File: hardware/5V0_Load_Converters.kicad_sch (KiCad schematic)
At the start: 77 parts, among them J19 61300311121, Q26 EPC2016C, Q27 EPC2016C, Q8 SI2302DDS-T1-GE3, U21 INA199C3DCKR, U30 LTC3833EUDC-TRPBF

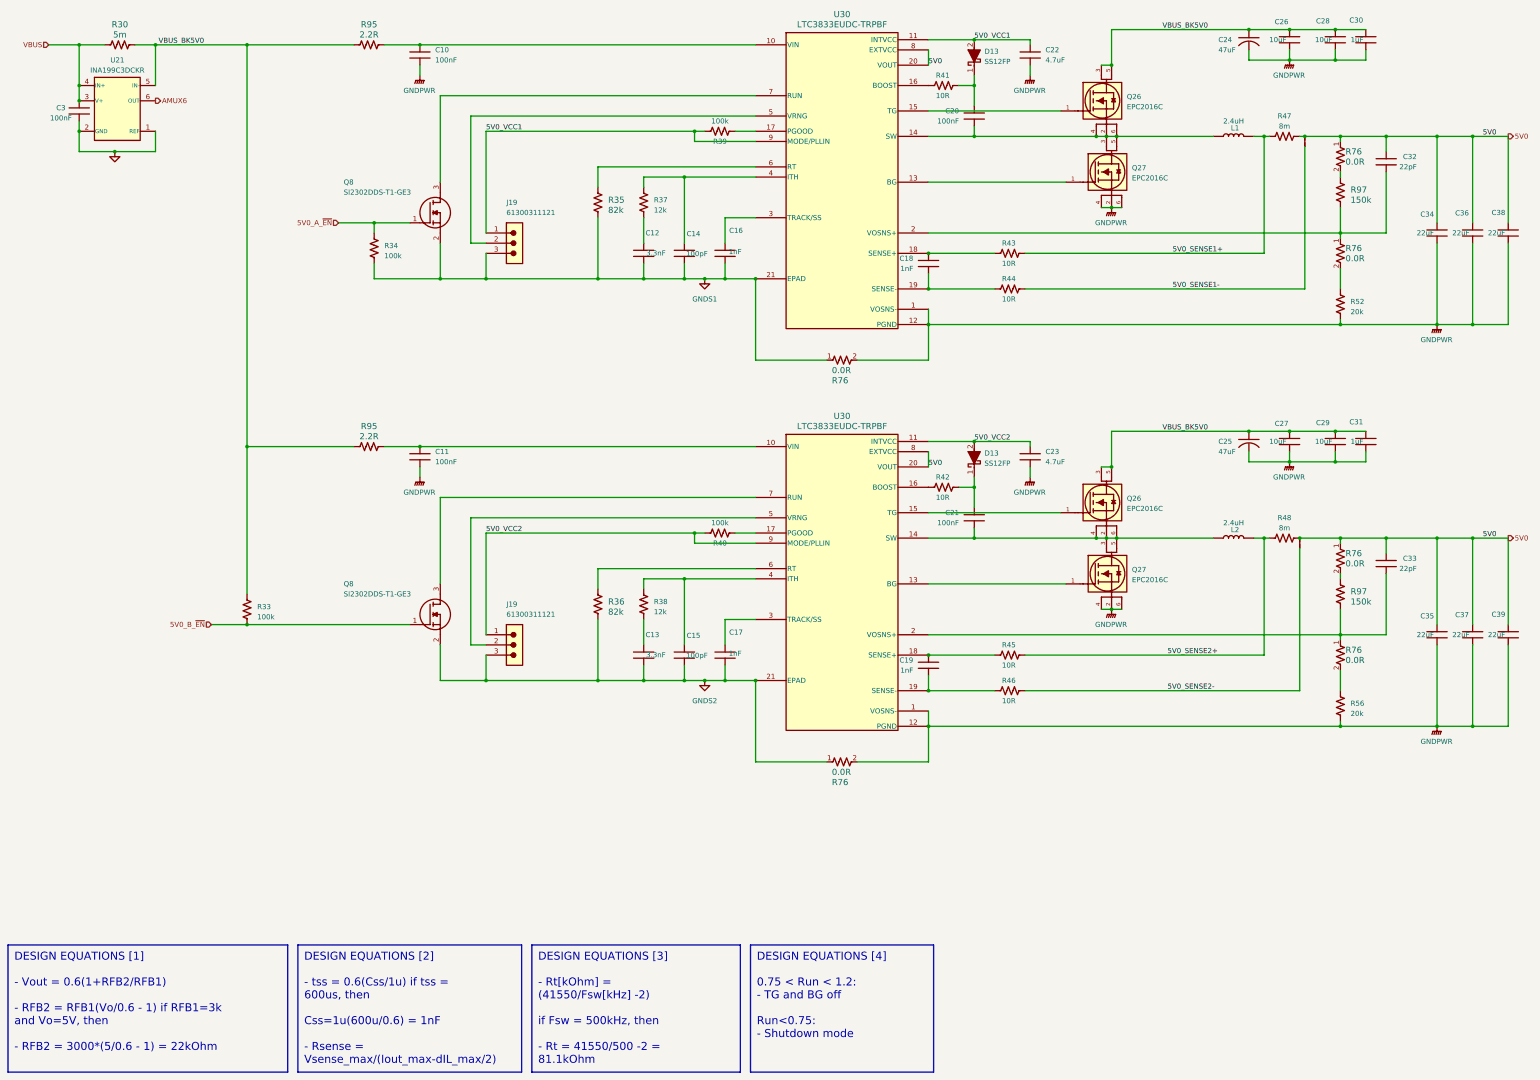
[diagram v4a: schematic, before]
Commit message: hardware: Updating the MPPT circuit.
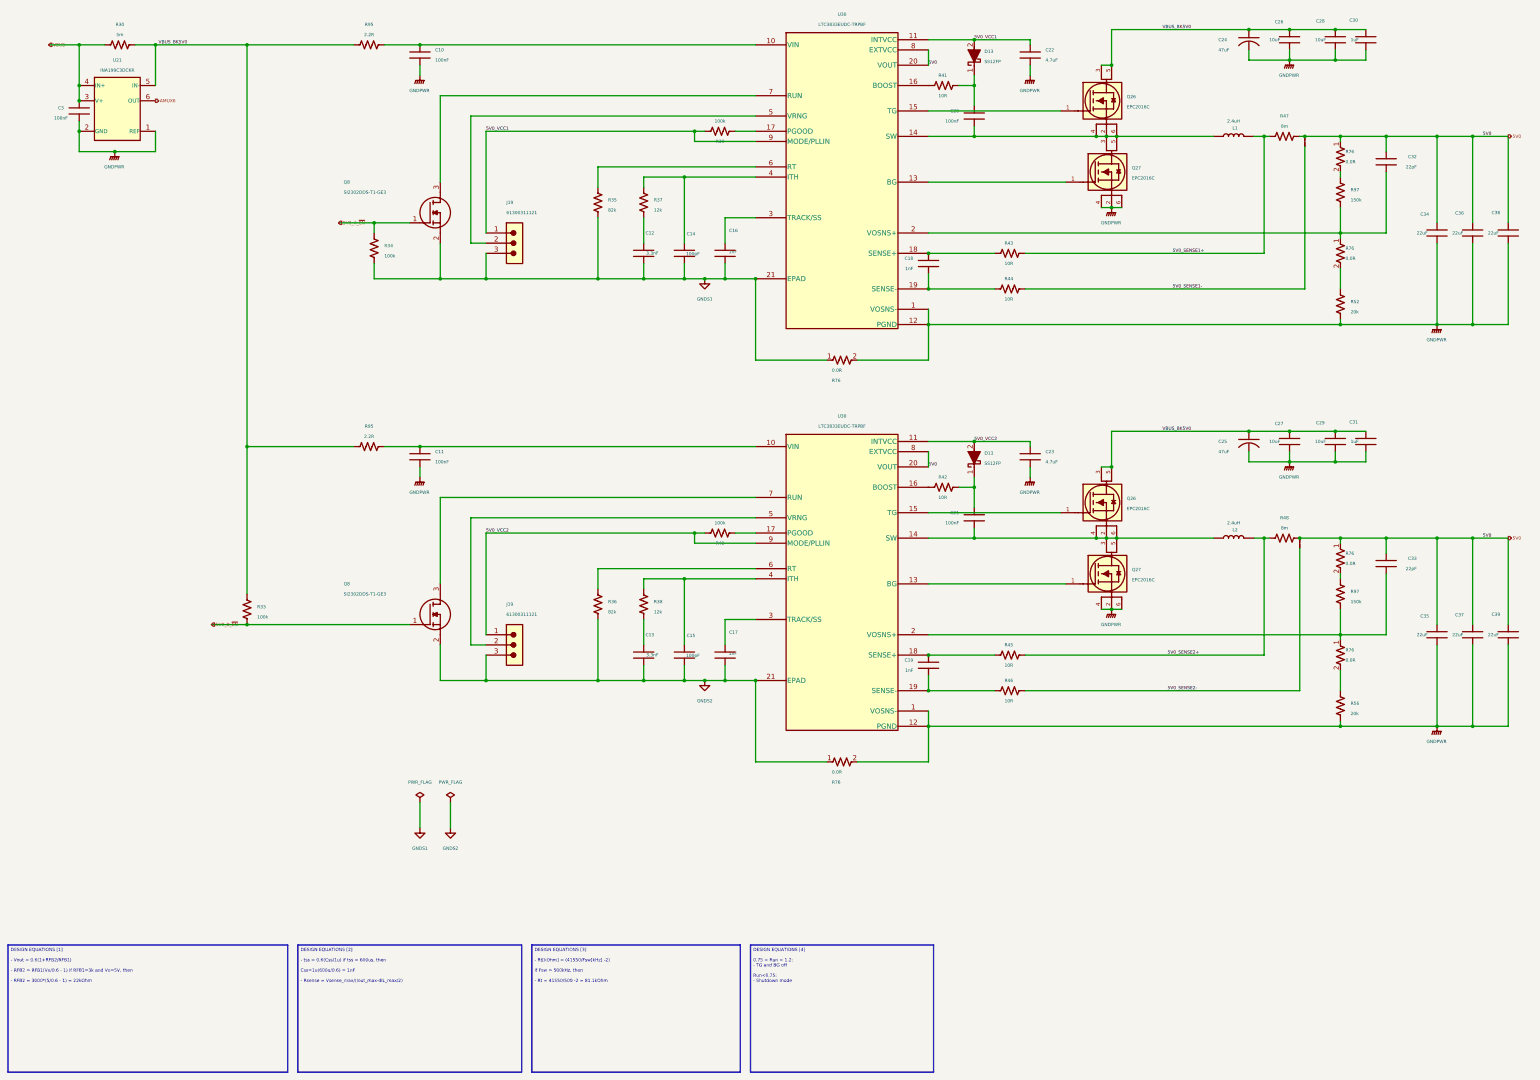
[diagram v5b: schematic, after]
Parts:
- JP1, JP2: symbol Jumper:Jumper -> JUMPER:JUMPER
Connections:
- net GND is gone; now on net GNDPWR: C3.2, U21.1 (REF), U21.2 (GND)

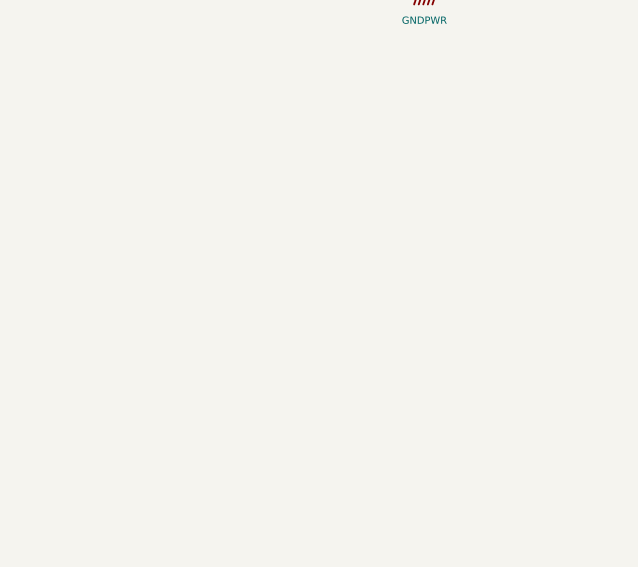
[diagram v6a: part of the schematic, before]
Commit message: hardware: Updating the custom design rules and library.
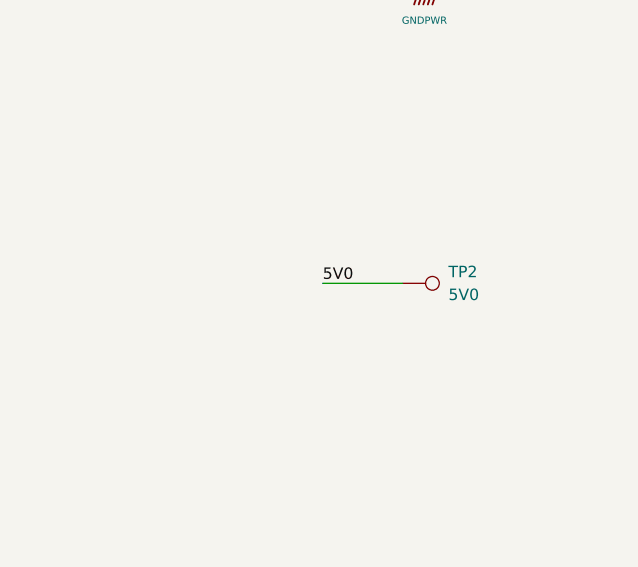
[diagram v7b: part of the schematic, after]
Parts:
- added TP2: 5V0, TestPoint:TestPoint_Pad_D1.0mm, symbol TESTPOINT:TestPoint
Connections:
- net 5V0: now also TP2.1
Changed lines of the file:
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@@
     (stroke (width 0) (type default))
   )
+  (wire (pts (xy 360.68 228.6) (xy 369.57 228.6))
+    (stroke (width 0.5) (type default))
+  )
   (wire (pts (xy 269.24 77.47) (xy 328.93 77.47))
     (stroke (width 0) (type default))
@@
     (effects (font (size 0.8 0.8)) (justify left bottom))
   )
+  (label "5V0" (at 360.68 228.6 0) (fields_autoplaced)
+    (effects (font (size 1.27 1.27)) (justify left bottom))
+  )
   (label "5V0" (at 245.11 130.81 0) (fields_autoplaced)
     (effects (font (size 0.8 0.8)) (justify left bottom))
@@
         )
       )
+    )
+  )
+  (symbol (lib_id "TESTPOINT:TestPoint") (at 369.57 228.6 270) (unit 1)
+    (in_bom yes) (on_board yes) (dnp no) (fields_autoplaced)
+    (property "Reference" "TP2" (at 374.65 227.33 90)
+      (effects (font (size 1.27 1.27)) (justify left))
+    )
+    (property "Value" "5V0" (at 374.65 229.87 90)
+      (effects (font (size 1.27 1.27)) (justify left))
+    )
+    (property "Footprint" "TestPoint:TestPoint_Pad_D1.0mm" (at 369.57 233.68 0)
+      (effects (font (size 1.27 1.27)) hide)
+    )
+    (property "Datasheet" "~" (at 369.57 233.68 0)
+      (effects (font (size 1.27 1.27)) hide)
+    )
+    (pin "1")
+    (instances
+      (project "eps-re_project"
+        (path "/2eebaa11-d7ed-4bfd-bc8e-988f68654d29/6f34948c-43a8-4614-b8ed-90c5b6b9b243"
+          (reference "TP2") (unit 1)
+        )
+        (path "/2eebaa11-d7ed-4bfd-bc8e-988f68654d29"
+          (reference "TP4") (unit 1)
+        )
+        (path "/2eebaa11-d7ed-4bfd-bc8e-988f68654d29/6cd5fe02-9b19-49bf-9109-b0a2c2f10c14"
+          (reference "TP4") (unit 1)
+        )
+      )

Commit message: hardware: Adding blocking diodes. Pass through diodes were also added in MPPT-based converters. Also, test points were added.
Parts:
- TP2: footprint TestPoint:TestPoint_Pad_D1.0mm -> footprints:testpoint_smd
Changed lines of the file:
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@@
       (effects (font (size 1.27 1.27)) (justify left))
     )
-    (property "Footprint" "TestPoint:TestPoint_Pad_D1.0mm" (at 369.57 233.68 0)
+    (property "Footprint" "footprints:testpoint_smd" (at 369.57 233.68 0)
       (effects (font (size 1.27 1.27)) hide)
     )
